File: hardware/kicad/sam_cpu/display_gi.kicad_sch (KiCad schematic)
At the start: 16 parts, among them J18 J18 GI DIMMER, J5 J5 DMD, U21 74HCT245

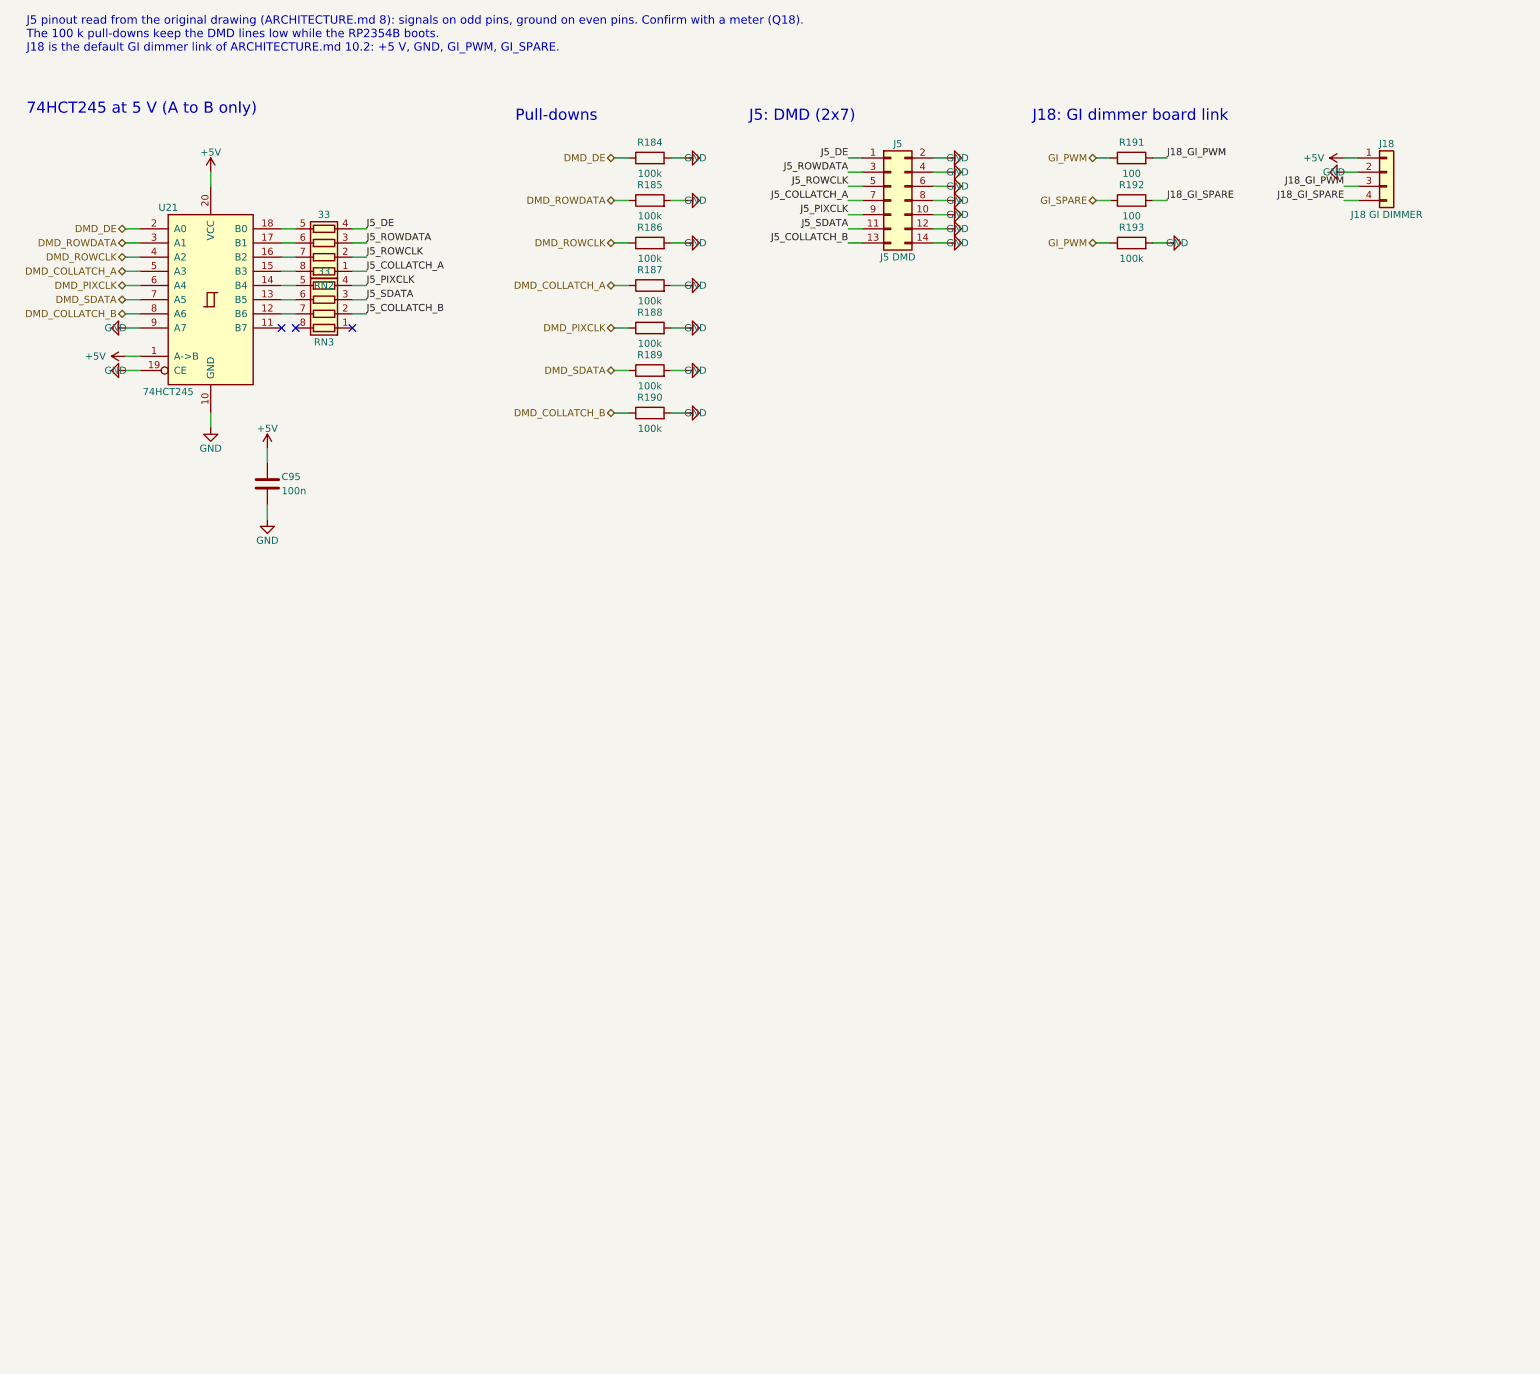
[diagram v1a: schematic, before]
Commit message: Redraw the schematic with wires (draft 0.2)
Every connection is now a wire, and each connector sits on the page of the
parts that drive or read it (Pi header with the RP2354B, J6/J12 with their
comparators and 74HC165, J1 with the 74HC595, J2/J3/J13 with their filters).
Signals between pages use global labels with page references. The Pi page is
merged into the MCU page; the Pi 4 sits on the 40-pin header J21.

ERC: 0 errors, 1 warning. Netlist check: 1266 pins, 299 nets, no differences.

Co-Authored-By: Claude Opus 5.5 (1M context) <noreply@anthropic.com>
Claude-Session: https://claude.ai/code/session_019DLTv1F2PjepjxqiUcAMKV
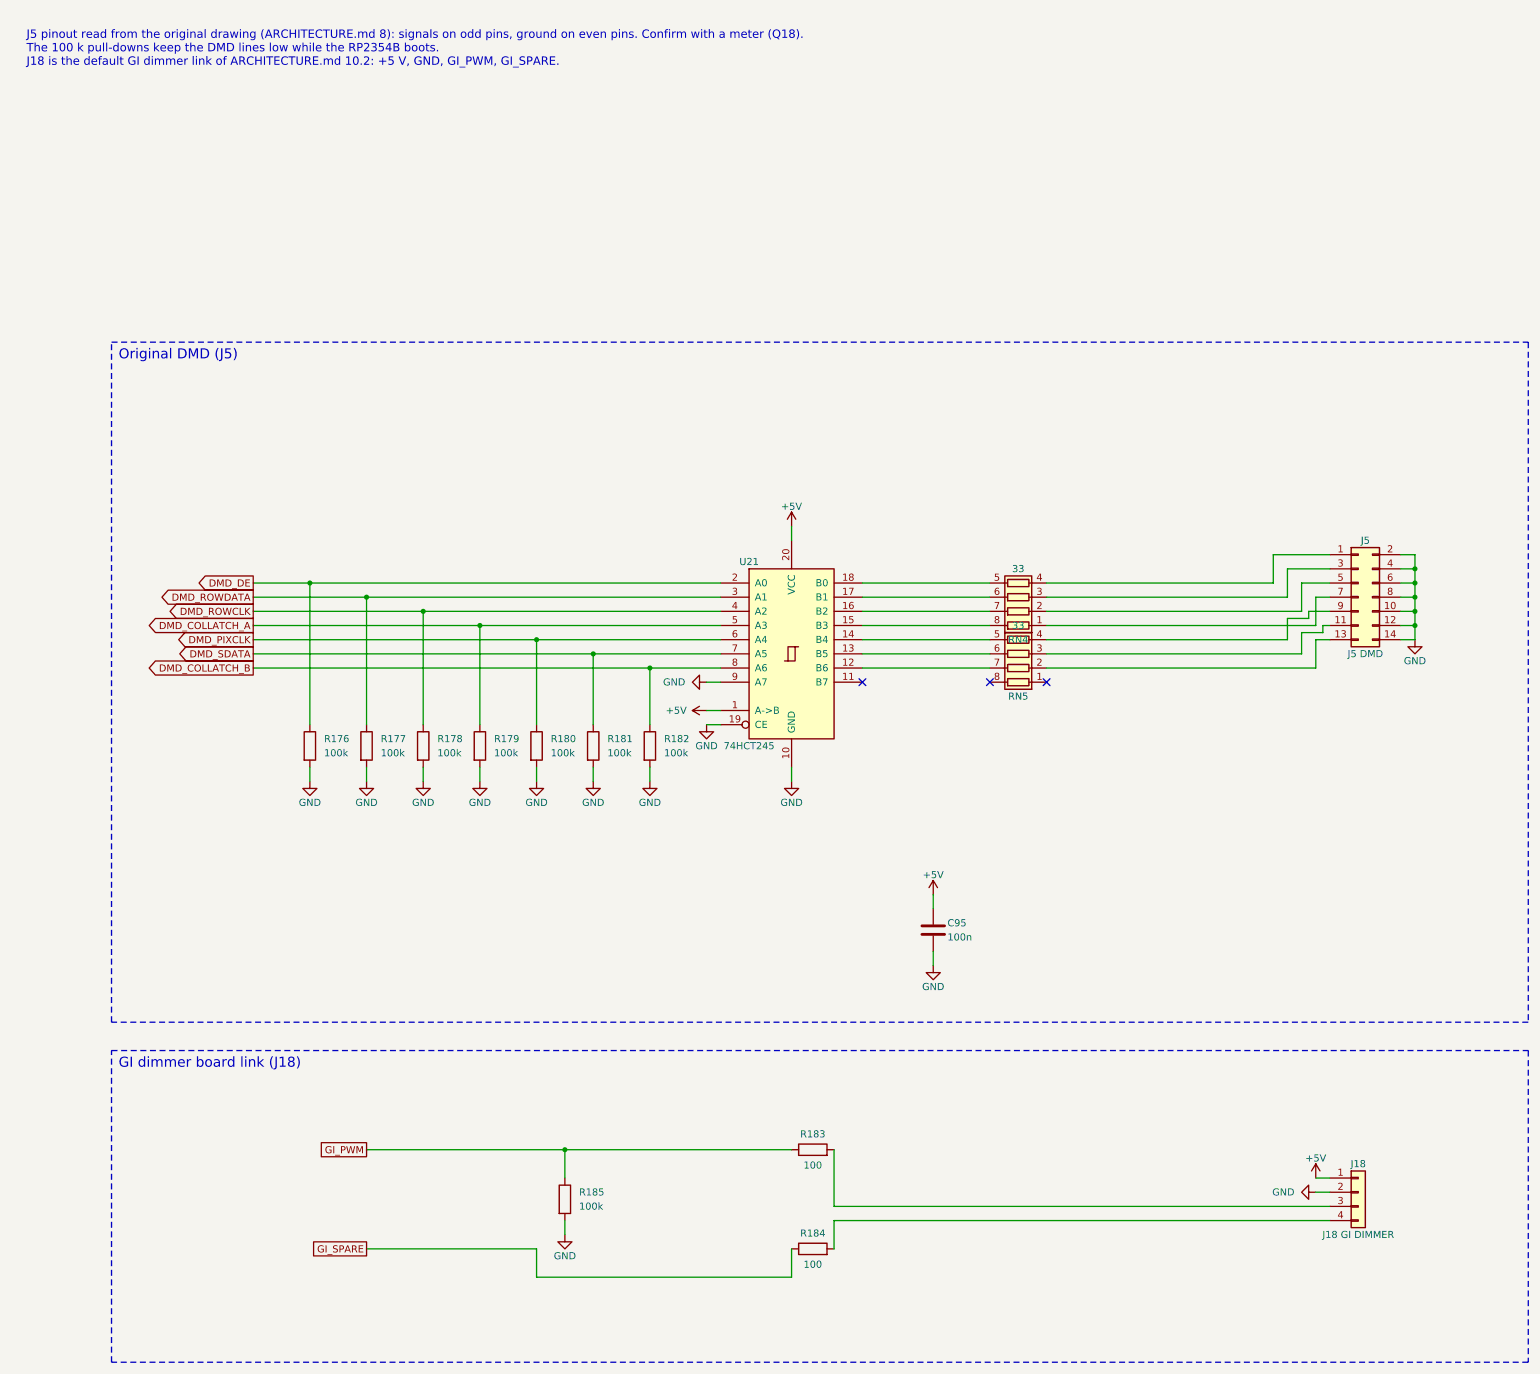
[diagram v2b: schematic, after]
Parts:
- removed R186, R187, R188, R189, R190, R193: 100k, Resistor_SMD:R_0603_1608Metric, symbol Device:R
- removed R191, R192: 100, Resistor_SMD:R_0603_1608Metric, symbol Device:R
- removed RN2, RN3: 33, Resistor_SMD:R_Array_Convex_4x0603, symbol Device:R_Pack04
- added R176, R177, R178, R179, R180, R181, R182: 100k, Resistor_SMD:R_0603_1608Metric, symbol Device:R
- added R183: 100, Resistor_SMD:R_0603_1608Metric, symbol Device:R
- added RN4, RN5: 33, Resistor_SMD:R_Array_Convex_4x0603, symbol Device:R_Pack04
- R184: value 100k -> 100
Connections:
- net DMD_COLLATCH_A: now also R179.1
- net DMD_COLLATCH_B: now also R182.1
- net DMD_DE: now also R176.1; no longer R184.1
- net DMD_PIXCLK: now also R180.1
- net DMD_ROWCLK: now also R178.1
- net DMD_ROWDATA: now also R177.1; no longer R185.1
- net DMD_SDATA: now also R181.1
- net GI_PWM: now also R185.1, R183.1
- net GI_SPARE: now also R184.1
- net GND: now also R176.2, R177.2, R178.2, R179.2, R180.2, R181.2, R182.2; no longer R184.2
- net at U21.12 (B6): now also RN5.7 (R2.2)
- net at U21.13 (B5): now also RN5.6 (R3.2)
- net at U21.14 (B4): now also RN5.5 (R4.2)
- net at U21.15 (B3): now also RN4.8 (R1.2)
- net at U21.16 (B2): now also RN4.7 (R2.2)
- net at U21.17 (B1): now also RN4.6 (R3.2)
- net at U21.18 (B0): now also RN4.5 (R4.2)
- net J18_GI_PWM: no longer names the net of J18.3 (Pin_3)
- net J18_GI_PWM: now also R183.2
- net J18_GI_SPARE: no longer names the net of J18.4 (Pin_4)
- net J18_GI_SPARE: now also R184.2
- net J5_COLLATCH_A: no longer names the net of J5.7 (Pin_7)
- net J5_COLLATCH_A: now also RN4.1 (R1.1)
- net J5_COLLATCH_B: no longer names the net of J5.13 (Pin_13)
- net J5_COLLATCH_B: now also RN5.2 (R2.1)
- net J5_DE: no longer names the net of J5.1 (Pin_1)
- net J5_DE: now also RN4.4 (R4.1)
- net J5_PIXCLK: no longer names the net of J5.9 (Pin_9)
- net J5_PIXCLK: now also RN5.4 (R4.1)
- net J5_ROWCLK: no longer names the net of J5.5 (Pin_5)
- net J5_ROWCLK: now also RN4.2 (R2.1)
- net J5_ROWDATA: no longer names the net of J5.3 (Pin_3)
- net J5_ROWDATA: now also RN4.3 (R3.1)
- net J5_SDATA: no longer names the net of J5.11 (Pin_11)
- net J5_SDATA: now also RN5.3 (R3.1)
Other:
- note added: "GI dimmer board link (J18)"
- note added: "Original DMD (J5)"
- note removed: "74HCT245 at 5 V (A to B only)"
- note removed: "J18: GI dimmer board link"
- note removed: "J5: DMD (2x7)"
- note removed: "Pull-downs"
- title: J5 original DMD driver and GI dimmer header -> J5 original DMD driver and J18 GI dimmer header
- moved on the sheet: C95, J18, J5, R184, R185, U21

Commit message: Add two HD DMD panels on a PIO parallel bus (incremental edit)
RP2354B GPIO20-36 drive two HUB75 panels (J25/J26) through 3 x 74AHCT245
with shared CLK/LAT/OE and A/B row lines; J5 shares DMD_D0-D6. The 165
load and 595 latch share GPIO17; coin door moves to a 7th 165 (U30),
LED_STATUS and GI_SPARE to a new first 595 (U31). Board widened to 142 mm
below the Pi. Sheets and board edited in place via tools/changes, no
existing footprint moved.

Co-Authored-By: Claude Opus 5.5 (1M context) <noreply@anthropic.com>
Claude-Session: https://claude.ai/code/session_01ExuDVoDDDHhVWjb8EwVzYb
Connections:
- net DMD_COLLATCH_A renamed DMD_D3
- net DMD_COLLATCH_B renamed DMD_D6
- net DMD_DE renamed DMD_D0
- net DMD_PIXCLK renamed DMD_D4
- net DMD_ROWCLK renamed DMD_D2
- net DMD_ROWDATA renamed DMD_D1
- net DMD_SDATA renamed DMD_D5
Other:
- note added: "J5 pinout read from the original drawing (ARCHITECTURE.md 8): signals on odd pins, ground on even pins. Confirm with a meter (Q18). The 100 k pull-downs keep the DMD lines low while the RP2354B boots. J5 shares GPIO20-26 (DMD_D0-D6) with the HD panel bus: J5 order DE, ROWDATA, ROWCLK, COLLATCH_A, PIXCLK, SDATA, COLLATCH_B = DMD_D0-D6. Only one display path runs at a time (PIO2 program chosen at b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"
- note removed: "J5 pinout read from the original drawing (ARCHITECTURE.md 8): signals on odd pins, ground on even pins. Confirm with a meter (Q18). The 100 k pull-downs keep the DMD lines low while the RP2354B boots. J18 is the default GI dimmer link of ARCHITECTURE.md 10.2: +5 V, GND, GI_PWM, GI_SPARE."
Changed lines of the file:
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@@
 		)
 	)
-	(text "J5 pinout read from the original drawing (ARCHITECTURE.md 8): signals on odd pins, ground on even pins. Confirm with a meter (Q18).\nThe 100 k pull-downs keep the DMD lines low while the RP2354B boots.\nJ18 is the default GI dimmer link of ARCHITECTURE.md 10.2: +5 V, GND, GI_PWM, GI_SPARE."
+	(text "J5 pinout read from the original drawing (ARCHITECTURE.md 8): signals on odd pins, ground on even pins. Confirm with a meter (Q18).\nThe 100 k pull-downs keep the DMD lines low while the RP2354B boots. J5 shares GPIO20-26 (DMD_D0-D6) with the HD panel bus: J5 order DE, ROWDATA, ROWCLK, COLLATCH_A, PIXCLK, SDATA, COLLATCH_B = DMD_D0-D6. Only one display path runs at a time (PIO2 program chosen at boot).\nJ18 is the default GI dimmer link of ARCHITECTURE.md 10.2: +5 V, GND, GI_PWM, GI_SPARE (GI_SPARE is now an on/off output of U31)."
 		(exclude_from_sim no)
 		(at 15.24 15.24 0)
@@
 		)
 	)
-	(global_label "DMD_ROWCLK"
+	(global_label "DMD_D2"
 		(shape output)
 		(at 55.88 119.38 180)
@@
 		)
 	)
-	(global_label "DMD_COLLATCH_A"
+	(global_label "DMD_D3"
 		(shape output)
 		(at 55.88 121.92 180)
@@
 		)
 	)
-	(global_label "DMD_DE"
+	(global_label "DMD_D0"
 		(shape output)
 		(at 55.88 114.3 180)
@@
 		)
 	)
-	(global_label "DMD_COLLATCH_B"
+	(global_label "DMD_D6"
 		(shape output)
 		(at 55.88 129.54 180)
@@
 		)
 	)
-	(global_label "DMD_ROWDATA"
+	(global_label "DMD_D1"
 		(shape output)
 		(at 55.88 116.84 180)
@@
 		)
 	)
-	(global_label "DMD_PIXCLK"
+	(global_label "DMD_D4"
 		(shape output)
 		(at 55.88 124.46 180)
@@
 		)
 	)
-	(global_label "DMD_SDATA"
+	(global_label "DMD_D5"
 		(shape output)
 		(at 55.88 127 180)

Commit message: Remove both DMD interfaces from the schematic and the board
DMD signals do not survive the long cabinet wires (Vincent, 2026-10-07).
Removed: J5 original DMD driver (U21, RN4, RN5, R176-R182, C95) and the
HD panel bus (J25, J26, U27-U29, RN6-RN11, C122-C124, TP23, TP24), their
tracks and fan-out vias. U30 / U31 stay (switch chain). RP2354B GPIO20-36
are unassigned (no-connect flags). The board goes back to the original
120.65 x 231.76 mm outline. DRC: 20 connections still open (was 35).

Co-Authored-By: Claude Opus 5.5 (1M context) <noreply@anthropic.com>
Claude-Session: https://claude.ai/code/session_01ExuDVoDDDHhVWjb8EwVzYb
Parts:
- removed C95: 100n, Capacitor_SMD:C_0603_1608Metric, symbol Device:C
- removed J5: J5 DMD, Connector_IDC:IDC-Header_2x07_P2.54mm_Vertical, symbol Connector_Generic:Conn_02x07_Odd_Even
- removed R176, R177, R178, R179, R180, R181, R182: 100k, Resistor_SMD:R_0603_1608Metric, symbol Device:R
- removed RN4, RN5: 33, Resistor_SMD:R_Array_Convex_4x0603, symbol Device:R_Pack04
- removed U21: 74HCT245, Package_SO:TSSOP-20_4.4x6.5mm_P0.65mm, symbol 74xx:74HC245
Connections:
- no-connect marks 3 -> 0
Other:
- note added: "J18 is the default GI dimmer link of ARCHITECTURE.md 10.2: +5 V, GND, GI_PWM, GI_SPARE (GI_SPARE is an on/off output of U31). The DMD interfaces were removed (2026-10-07): DMD signals do not survive the long cabinet wires."
- note removed: "J5 pinout read from the original drawing (ARCHITECTURE.md 8): signals on odd pins, ground on even pins. Confirm with a meter (Q18). The 100 k pull-downs keep the DMD lines low while the RP2354B boots. J5 shares GPIO20-26 (DMD_D0-D6) with the HD panel bus: J5 order DE, ROWDATA, ROWCLK, COLLATCH_A, PIXCLK, SDATA, COLLATCH_B = DMD_D0-D6. Only one display path runs at a time (PIO2 program chosen at b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"
- note removed: "Original DMD (J5)"

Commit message: Add an RS485 port (RJ45) and an I2S input header
Vincent, 2026-10-07: one RS485 port for both set-ups. With the Pi on J21
it is the Pi's UART3 (GPIO4 / 5, RTS on GPIO7 as driver enable); with a
remote Pi it is the RP2354B's UART1 (GPIO20 / 21, GPIO22 driver enable),
and the remote Pi's I2S reaches the DAC on J28. Both sides reach the
THVD1450 through 1 k, so only the configured side drives.

New page 13 (U32, R204-R212, C127, D27, JP2, J27, J28), RS485 labels on
the MCU sheet, and the 15 footprints placed without moving any part: the
RJ45 on the right edge where J5 was. README / PCB.md updated for draft 0.6
(DMD removal included). ERC clean; the new nets are not routed yet.

Co-Authored-By: Claude Opus 5.5 (1M context) <noreply@anthropic.com>
Claude-Session: https://claude.ai/code/session_01ExuDVoDDDHhVWjb8EwVzYb
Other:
- title: J5 original DMD driver and J18 GI dimmer header -> J18 GI dimmer header
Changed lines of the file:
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@@
 	(paper "A3")
 	(title_block
-		(title "J5 original DMD driver and J18 GI dimmer header")
+		(title "J18 GI dimmer header")
 		(date "2026-10-06")
 		(rev "0.2")
